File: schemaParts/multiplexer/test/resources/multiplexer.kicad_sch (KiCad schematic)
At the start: 6 parts

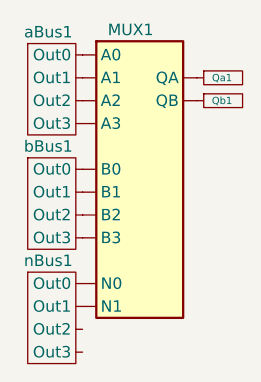
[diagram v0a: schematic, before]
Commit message: Masked multiplexer Map 74LS157, 74LS153
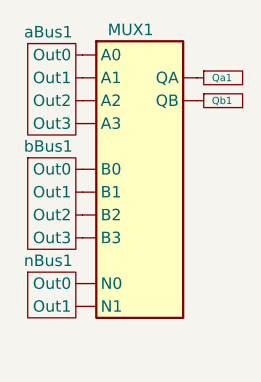
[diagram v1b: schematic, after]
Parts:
- removed nBus1: OutBus4x, symbol Tests:OutBus4x
- added nBus1: OutBus2x, symbol Tests:OutBus2x
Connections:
- net at MUX1.1 (N0): now also nBus1.0 (Out0)
- net at MUX1.2 (N1): now also nBus1.1 (Out1)
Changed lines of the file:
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@@
+    )
+  )
+  (symbol (lib_id "Tests:OutBus2x") (at 133.35 73.66 0) (unit 1)
+    (in_bom yes) (on_board yes) (dnp no)
+    (property "Reference" "nBus1" (at 129.54 69.85 0)
+      (effects (font (size 1.27 1.27)))
+    )
+    (property "Value" "OutBus2x" (at 121.92 68.072 0)
+      (effects (font (size 1.27 1.27)) hide)
+    )
+    (property "Footprint" "" (at 132.6 78.74 0)
+      (effects (font (size 1.27 1.27)) hide)
+    )
+    (property "Datasheet" "" (at 132.6 78.74 0)
+      (effects (font (size 1.27 1.27)) hide)
+    )
+    (pin "1")
+    (pin "0")
+    (instances
+      (project "multiplexer"
+        (path "/dca00733-6e59-4b89-b3a6-bb50926963b6"
+          (reference "nBus1") (unit 1)
+        )
+      )
     )
   )
@@
         )
       )
-    )
-  )
-  (symbol (lib_id "Tests:OutBus4x") (at 133.35 76.2 0) (unit 1)
-    (in_bom yes) (on_board yes) (dnp no)
-    (property "Reference" "nBus1" (at 129.54 69.85 0)
-      (effects (font (size 1.27 1.27)))
-    )
-    (property "Value" "OutBus4x" (at 122.948 70.866 0)
-      (effects (font (size 1.27 1.27)) hide)
-    )
-    (property "Footprint" "" (at 132.6 81.28 0)
-      (effects (font (size 1.27 1.27)) hide)
-    )
-    (property "Datasheet" "" (at 132.6 81.28 0)
-      (effects (font (size 1.27 1.27)) hide)
-    )
-    (pin "3")
-    (pin "1")
-    (pin "2")
-    (pin "0")
-    (instances
-      (project "multiplexer"
-        (path "/dca00733-6e59-4b89-b3a6-bb50926963b6"
-          (reference "nBus1") (unit 1)
-        )
-      )
